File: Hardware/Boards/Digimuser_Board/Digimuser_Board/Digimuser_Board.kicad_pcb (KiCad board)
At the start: 2 copper layers, 63 parts, among them J1 Conn_01x01, J10 Conn_01x01, J11 Conn_01x01, J12 Conn_01x01, J2 Conn_01x01, J3 Barrel_Jack, J4 Conn_01x03, J5 Conn_01x03, J6 Conn_01x01, J7 Conn_01x01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

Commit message: Started the PCB layout. Also had to find a new voltage regulator.
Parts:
- removed H4: MountingHole_Pad, MountingHole:MountingHole_3.2mm_M3_Pad
- added C22: 0.33u, Capacitor_SMD:C_0805_2012Metric, F.Cu at (118.9, 69.3)
- added C23: 0.1u, Capacitor_SMD:C_0805_2012Metric, F.Cu at (121.2, 79.0)
- H1, H2, H3: footprint MountingHole:MountingHole_3.2mm_M3_Pad -> MountingHole:MountingHole_2.2mm_M2_Pad
- J3: value Barrel_Jack -> Barrel_Jack_MountingPin
- U2: value AMS1117CD-5.0 -> UA78M05IDCYR; footprint Package_TO_SOT_SMD:TO-252-3_TabPin2 -> Package_TO_SOT_SMD:SOT-223
- moved H1 80.9 mm to (165.7, 69.8)
- moved H2 65.8 mm to (165.7, 102.2)
- moved H3 31.2 mm to (104.8, 102.2)
- moved U2 7.67 mm to (123.4, 74.2)
- moved U4 6.43 mm to (120.0, 89.5)
- moved J3 6.30 mm to (115.6, 73.0)
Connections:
- J3 pad 1: Net-(J3-Pad1) -> Net-(C22-Pad1)
- J3 pad 3: (no net) -> GND
- U2 pad 1: GND -> Net-(C22-Pad1)
- U2 pad 2: 5V -> GND
- U2 pad 3: Net-(J3-Pad1) -> 5V
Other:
- board outline added: 67.3 x 38.7 mm

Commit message: Completed most of the PCB layout organization. Still have a lot of work on it.
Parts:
- J1: footprint Connector_PinSocket_2.54mm:PinSocket_1x01_P2.54mm_Vertical -> Connector_PinHeader_2.54mm:PinHeader_1x01_P2.54mm_Vertical
- J10, J11, J12, J6, J7, J8, J9: footprint Connector_Pin:Pin_D1.3mm_L11.0mm_LooseFit -> Connector_PinHeader_2.54mm:PinHeader_1x01_P2.54mm_Vertical
- U4: footprint teensy:Teensy40 -> teensy:Teensy40_HAT
- moved C1 89.2 mm to (130.3, 73.4), turned to 90 degrees
- moved R9 73.1 mm to (138.2, 73.7), turned to 180 degrees
- moved C14 68.0 mm to (146.8, 81.3), turned to 90 degrees
- moved R1 65.0 mm to (130.0, 76.5)
- moved C3 63.8 mm to (137.4, 70.4), turned to 90 degrees
- moved R6 63.4 mm to (134.1, 78.5), turned to 270 degrees
- moved C2 63.3 mm to (137.7, 79.2)
- moved J12 61.4 mm to (117.1, 102.1), turned to 90 degrees
- moved C4 61.4 mm to (148.1, 69.8), turned to 180 degrees
- moved U5 60.7 mm to (176.5, 100.2)
- moved R10 59.7 mm to (139.7, 70.4), turned to 270 degrees
- moved C6 58.3 mm to (149.9, 74.9), turned to 270 degrees
- moved C5 58.2 mm to (144.0, 78.0), turned to 180 degrees
- moved R2 57.6 mm to (131.1, 78.7), turned to 180 degrees
- moved C7 56.5 mm to (139.4, 96.4), turned to 270 degrees
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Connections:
- net Net-(C22-Pad1) renamed /+9V
- C16 pad 1: Net-(C16-Pad1) -> 3.3V
- C19 pad 1: Net-(C16-Pad1) -> 3.3V
- J3 pad 3: GND -> (no net)
- U4 pad 31: (no net) -> 3.3V
- U6 pad 4: (no net) -> MCLK
- U7 pad 9: Net-(C16-Pad1) -> 3.3V
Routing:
- net MCLK: track 0.00 -> 31.7 mm
- net SCLK: track 0.00 -> 25.9 mm
- net LRCK: track 0.00 -> 25.7 mm, vias 0 -> 1
- net 3.3V: track 0.00 -> 23.9 mm
- net SDOUT: track 0.00 -> 23.9 mm, vias 0 -> 1
- net 5V: track 0.00 -> 20.5 mm
- net Net-(C17-Pad1): track 0.00 -> 11.8 mm, vias 0 -> 2
- net Net-(J6-Pad1): track 0.00 -> 11.6 mm
- net /+9V: track 0.00 -> 9.03 mm
- net /FILT_OUT: track 0.00 -> 8.15 mm
- net ADC_IN: track 0.00 -> 7.47 mm
- net Net-(C15-Pad2): track 0.00 -> 5.39 mm
- net Net-(C11-Pad1): track 0.00 -> 4.28 mm
- net Net-(C5-Pad1): track 0.00 -> 4.20 mm
- net Net-(C6-Pad2): track 0.00 -> 2.56 mm
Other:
- net class 2_SIGNAL_SDSU_MILL added: clearance 0.2, trace_width 0.7, via_dia 1.4, via_drill 0.7
- net class JLCPWR added: clearance 0.3, trace_width 0.4, via_dia 1, via_drill 0.5
- net class PWR_SDSU_MILL added: clearance 0.9, trace_width 1.27, via_dia 1.4, via_drill 0.7
- net class SIGNAL_SDSU_MILL added: clearance 0.9, trace_width 0.7, via_dia 1.4, via_drill 0.7
- net class SMALLSIG added: clearance 0.1, trace_width 0.2, via_dia 0.5, via_drill 0.3

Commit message: Continued PCB layout.
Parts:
- C13: footprint Capacitor_THT:CP_Radial_D6.3mm_P2.50mm -> Capacitor_THT:C_Axial_L5.1mm_D3.1mm_P7.50mm_Horizontal
- U1: footprint Connector_PinSocket_2.54mm:PinSocket_1x04_P2.54mm_Vertical -> Connector_PinSocket_2.54mm:PinSocket_1x05_P2.54mm_Vertical
- moved R3 77.9 mm to (126.6, 85.9), turned to 270 degrees
- moved R4 76.5 mm to (128.9, 85.9), turned to 270 degrees
- moved R5 66.2 mm to (131.4, 85.9), turned to 270 degrees
- moved R7 65.8 mm to (134.0, 85.8), turned to 270 degrees
- moved R8 62.2 mm to (136.7, 85.8), turned to 270 degrees
- moved C12 51.8 mm to (145.3, 98.0), turned to 90 degrees
- moved J8 45.8 mm to (124.5, 102.1)
- moved R15 40.1 mm to (154.0, 100.1), turned to 90 degrees
- moved R17 39.9 mm to (150.8, 100.6)
- moved C9 39.7 mm to (153.0, 95.1), turned to 270 degrees
- moved U5 27.2 mm to (149.5, 97.0)
- moved U1 23.9 mm to (126.4, 78.9)
- moved J9 11.3 mm to (120.8, 102.1)
- moved C22 8.32 mm to (117.9, 77.6), turned to 270 degrees
- moved R14 7.74 mm to (159.8, 77.7), turned to 90 degrees
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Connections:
- U1 pad 1: Net-(R7-Pad1) -> Net-(R3-Pad1)
- U1 pad 2: Net-(R5-Pad1) -> Net-(R4-Pad1)
- U1 pad 3: Net-(R4-Pad1) -> Net-(R5-Pad1)
- U1 pad 4: Net-(R3-Pad1) -> Net-(R7-Pad1)
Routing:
- net 5V: track 20.5 -> 0.00 mm
- net Net-(C12-Pad1): track 0.00 -> 13.3 mm
- net DAC_OUT: track 0.00 -> 12.2 mm, vias 0 -> 2
- net /AMP_IN: track 0.00 -> 12.1 mm
- net Net-(C2-Pad1): track 0.00 -> 10.1 mm
- net Net-(C12-Pad2): track 0.00 -> 9.50 mm
- net /+9V: track 9.03 -> 0.13 mm
- net Net-(R15-Pad2): track 0.00 -> 6.34 mm
- net Net-(R5-Pad1): track 0.00 -> 6.13 mm
- net Net-(R4-Pad1): track 0.00 -> 6.13 mm
- net Net-(R3-Pad1): track 0.00 -> 6.10 mm
- net Net-(R7-Pad1): track 0.00 -> 6.04 mm
- net Net-(R8-Pad1): track 0.00 -> 5.97 mm
- net Net-(R10-Pad2): track 0.00 -> 5.55 mm
- net Net-(C10-Pad1): track 0.00 -> 5.10 mm
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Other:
- board size 67.3 x 38.7 mm -> 60.2 x 38.7 mm

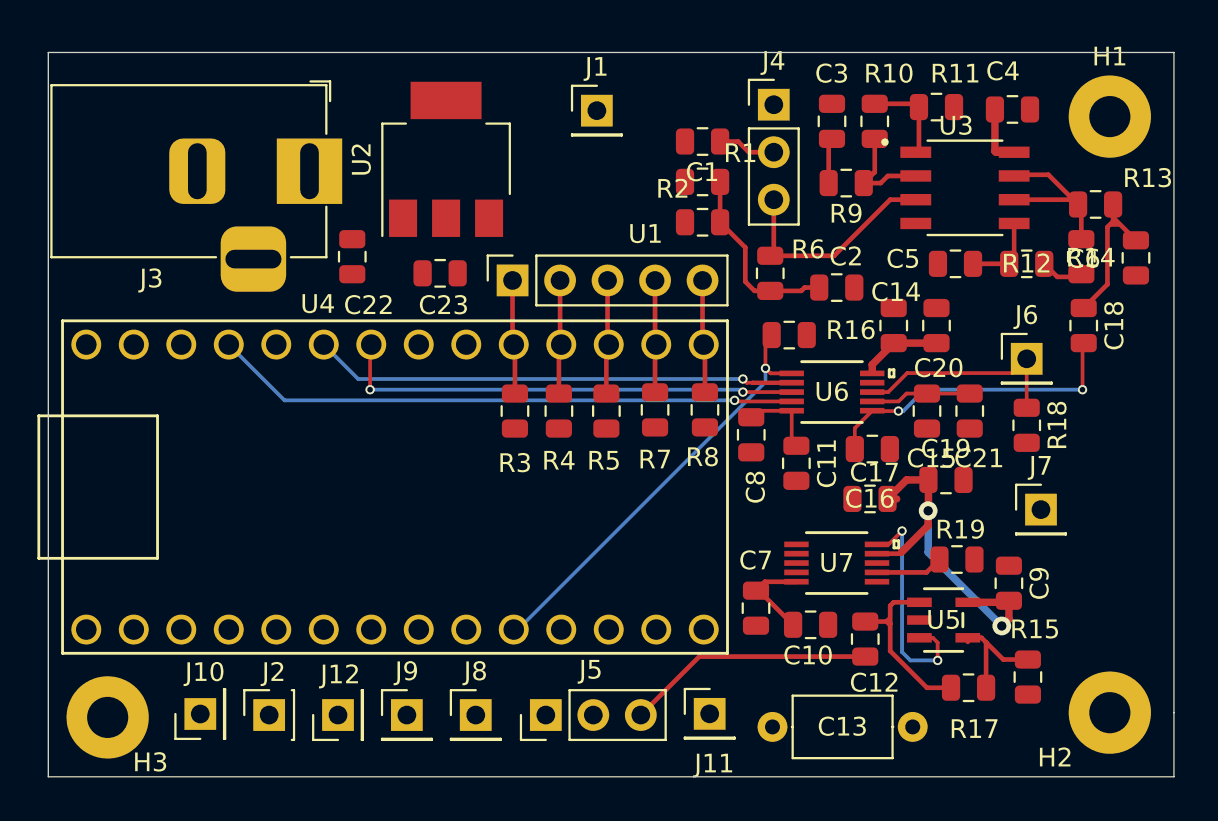
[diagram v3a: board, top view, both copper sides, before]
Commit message: Finished the first revision of the PCB layout. Needs reviewing.
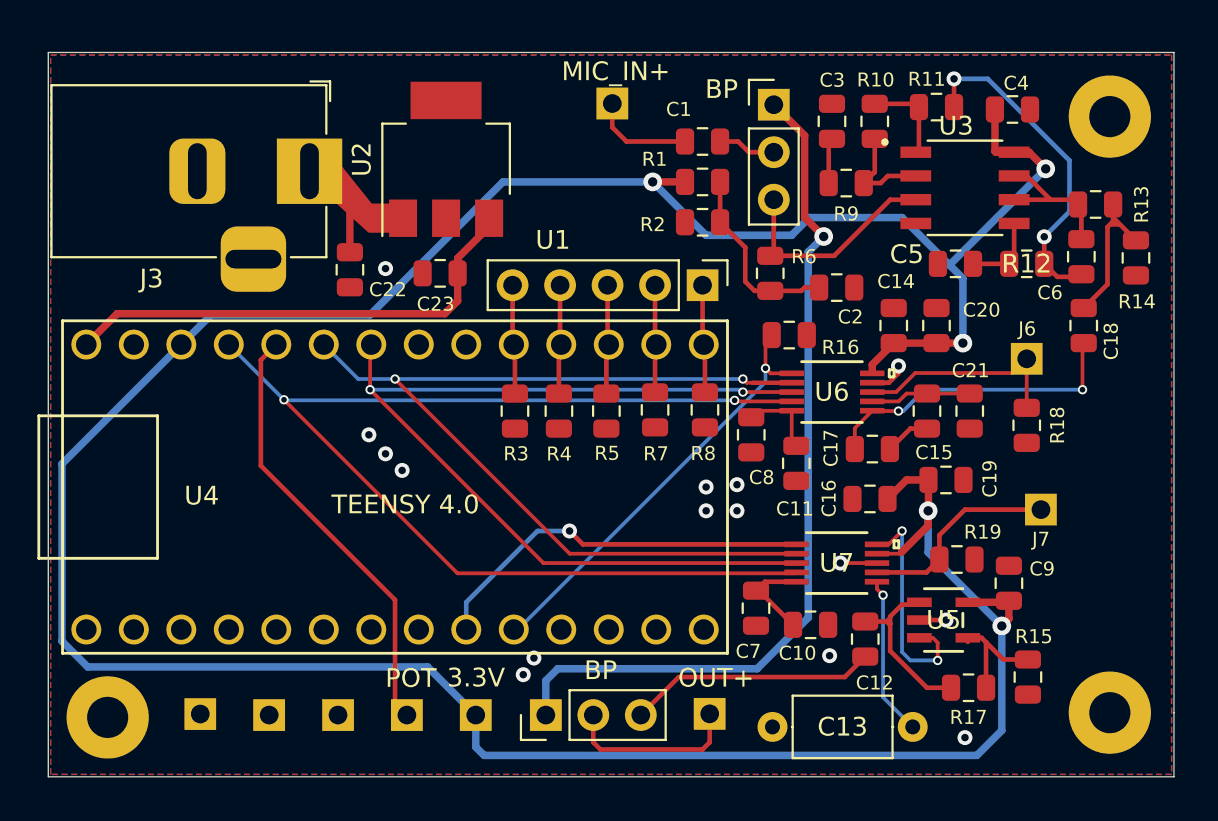
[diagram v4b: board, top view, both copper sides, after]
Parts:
- J1, J10, J11, J12, J6, J7, J8, J9: footprint Connector_PinHeader_2.54mm:PinHeader_1x01_P2.54mm_Vertical -> Custom_Connectors:PinHeader_2.54mm_1x01_P2.54mm
- J2: footprint Connector_PinSocket_2.54mm:PinSocket_1x01_P2.54mm_Vertical -> Custom_Connectors:PinHeader_2.54mm_1x01_P2.54mm
- J4, J5: footprint Connector_PinHeader_2.54mm:PinHeader_1x03_P2.54mm_Vertical -> Custom_Connectors:PinHeader_2.54mm_1x03_P2.54mm
- U1: footprint Connector_PinSocket_2.54mm:PinSocket_1x05_P2.54mm_Vertical -> Custom_Connectors:R20407RR02Q
- U7: value CS4344-CZZ -> (none)
- moved U1 10.2 mm to (136.6, 79.1), turned to 270 degrees
- moved J1 0.91 mm to (131.8, 69.4)
- moved C22 0.71 mm to (117.7, 78.3)
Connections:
- U1 pad 1: Net-(R3-Pad1) -> Net-(R7-Pad1)
- U1 pad 2: Net-(R4-Pad1) -> Net-(R5-Pad1)
- U1 pad 3: Net-(R5-Pad1) -> Net-(R4-Pad1)
- U1 pad 4: Net-(R7-Pad1) -> Net-(R3-Pad1)
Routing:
- net 3.3V: track 27.9 -> 170.2 mm, vias 2 -> 5
- net BYPASS: track 0.00 -> 46.1 mm, vias 0 -> 1
- net MCLK: track 31.4 -> 62.6 mm, vias 1 -> 2
- net LRCK: track 25.1 -> 51.7 mm
- net 5V: track 0.00 -> 25.9 mm
- net SCLK: track 27.3 -> 52.6 mm, vias 1 -> 2
- net Net-(J9-Pad1): track 0.00 -> 23.4 mm
- net SDIN: track 0.00 -> 21.0 mm, vias 0 -> 1
- net Net-(C6-Pad2): track 2.33 -> 18.0 mm, vias 0 -> 2
- net /+9V: track 0.13 -> 10.5 mm
- net Net-(J11-Pad1): track 0.00 -> 9.52 mm
- net Net-(C13-Pad1): track 0.00 -> 8.55 mm, vias 0 -> 1
- net GND: track 0.00 -> 7.82 mm, vias 0 -> 15
- net Net-(J7-Pad1): track 3.62 -> 10.9 mm
- net Net-(C1-Pad2): track 0.00 -> 5.47 mm
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- added copper zone on B.Cu, net GND
- added copper zone on F.Cu, net GND
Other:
- net class JLCPWR: clearance 0.3 -> 0.2
- board text added: "3.3V"
- board text added: "BP"
- board text added: "MIC_IN+"
- board text added: "OUT+"
- board text added: "POT"
- board text added: "TEENSY 4.0"

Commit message: Did a re-layout of the PCB and redid the schematic.Ready for review.
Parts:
- removed U5: MCP6271T-E_OT, MCP6271TE0T:MCP6271T-E&slash_OT
- added C24: 3.9n, Capacitor_SMD:C_0805_2012Metric, F.Cu at (157.3, 91.8)
- added C25: 3.9n, Capacitor_SMD:C_0805_2012Metric, F.Cu at (157.4, 95.5)
- added C26: 1u, Capacitor_SMD:C_0805_2012Metric, F.Cu at (155.2, 81.9)
- added C27: 180p, Capacitor_SMD:C_0805_2012Metric, F.Cu at (152.5, 81.9)
- added TP1: FILTIN, TestPoint:TestPoint_Keystone_5019_Minature, B.Cu at (146.8, 71.6)
- added TP2: FILTOUT, TestPoint:TestPoint_Keystone_5019_Minature, B.Cu at (153.6, 78.7)
- added TP3: AOUTR, TestPoint:TestPoint_Keystone_5019_Minature, B.Cu at (145.4, 89.7)
- added TP4: AOUTL, TestPoint:TestPoint_Keystone_5019_Minature, B.Cu at (146.3, 96.5)
- C12: value ? -> 3.3u
- C9: value 0.1u -> 3.3u
- R15: value 1K -> 10K
- R17: value 5K -> 10K
- R18: value 0 -> 470
- R19: value 10K -> 470
- U7: value (none) -> CS4344-CZZ
- moved J11 8.85 mm to (128.1, 102.1)
- moved R15 8.26 mm to (153.3, 91.8)
- moved J5 7.33 mm to (135.5, 102.1)
- moved C12 5.99 mm to (150.4, 94.9), turned to 180 degrees
- moved J7 5.92 mm to (158.9, 86.9)
- moved R17 5.70 mm to (153.3, 95.5), turned to 270 degrees
- moved R18 5.41 mm to (155.3, 91.8)
- moved R19 5.38 mm to (155.3, 95.5), turned to 90 degrees
- moved J6 4.06 mm to (155.2, 86.9)
- moved C13 3.78 mm to (146.6, 99.2), turned to 0 degrees
- moved C9 3.42 mm to (150.4, 92.8), turned to 180 degrees
- moved C18 0.66 mm to (157.6, 81.2)
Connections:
- C9 pad 1: GND -> Net-(C9-Pad1)
- C9 pad 2: 3.3V -> Net-(C9-Pad2)
- J5 pad 3: Net-(C12-Pad1) -> Net-(C25-Pad1)
- J6 pad 1: Net-(J6-Pad1) -> Net-(C26-Pad1)
- J7 pad 1: Net-(J7-Pad1) -> Net-(C24-Pad1)
- R15 pad 1: GND -> Net-(C9-Pad1)
- R15 pad 2: Net-(R15-Pad2) -> GND
- R17 pad 1: Net-(C12-Pad2) -> Net-(C12-Pad1)
- R17 pad 2: Net-(R15-Pad2) -> GND
- R18 pad 1: Net-(J6-Pad1) -> Net-(C24-Pad1)
- R18 pad 2: GND -> Net-(C9-Pad1)
- R19 pad 1: Net-(J7-Pad1) -> Net-(C25-Pad1)
- R19 pad 2: GND -> Net-(C12-Pad1)
- U6 pad 8: Net-(J6-Pad1) -> Net-(C26-Pad2)
- U7 pad 10: DAC_OUT -> Net-(C9-Pad2)
- U7 pad 7: Net-(J7-Pad1) -> Net-(C12-Pad2)
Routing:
- net Net-(C25-Pad1): track 0.00 -> 21.7 mm
- net DAC_OUT: track 12.2 -> 0.00 mm, vias 2 -> 0
- net Net-(C26-Pad2): track 0.00 -> 12.0 mm
- net Net-(J6-Pad1): track 11.6 -> 0.00 mm
- net Net-(J7-Pad1): track 10.9 -> 0.00 mm
- net BYPASS: track 46.1 -> 36.8 mm
- net Net-(C12-Pad1): track 13.3 -> 4.20 mm
- net Net-(C9-Pad2): track 0.00 -> 8.10 mm, vias 0 -> 1
- net Net-(C24-Pad1): track 0.00 -> 6.65 mm
- net Net-(R15-Pad2): track 6.34 -> 0.00 mm
- net /FILT_IN: track 4.92 -> 9.94 mm, vias 0 -> 1
- net /FILT_OUT: track 8.01 -> 13.0 mm, vias 0 -> 1
- net Net-(C26-Pad1): track 0.00 -> 4.11 mm
- net Net-(C13-Pad1): track 8.55 -> 4.47 mm, vias 1 -> 0
- net Net-(C9-Pad1): track 0.00 -> 3.93 mm
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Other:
- board text added: "GND"

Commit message: Relabled Testpoints on PCB.
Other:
- board text added: "AOUTL"
- board text added: "AOUTR"
- board text added: "FILTIN"
- board text added: "FILTOUT"

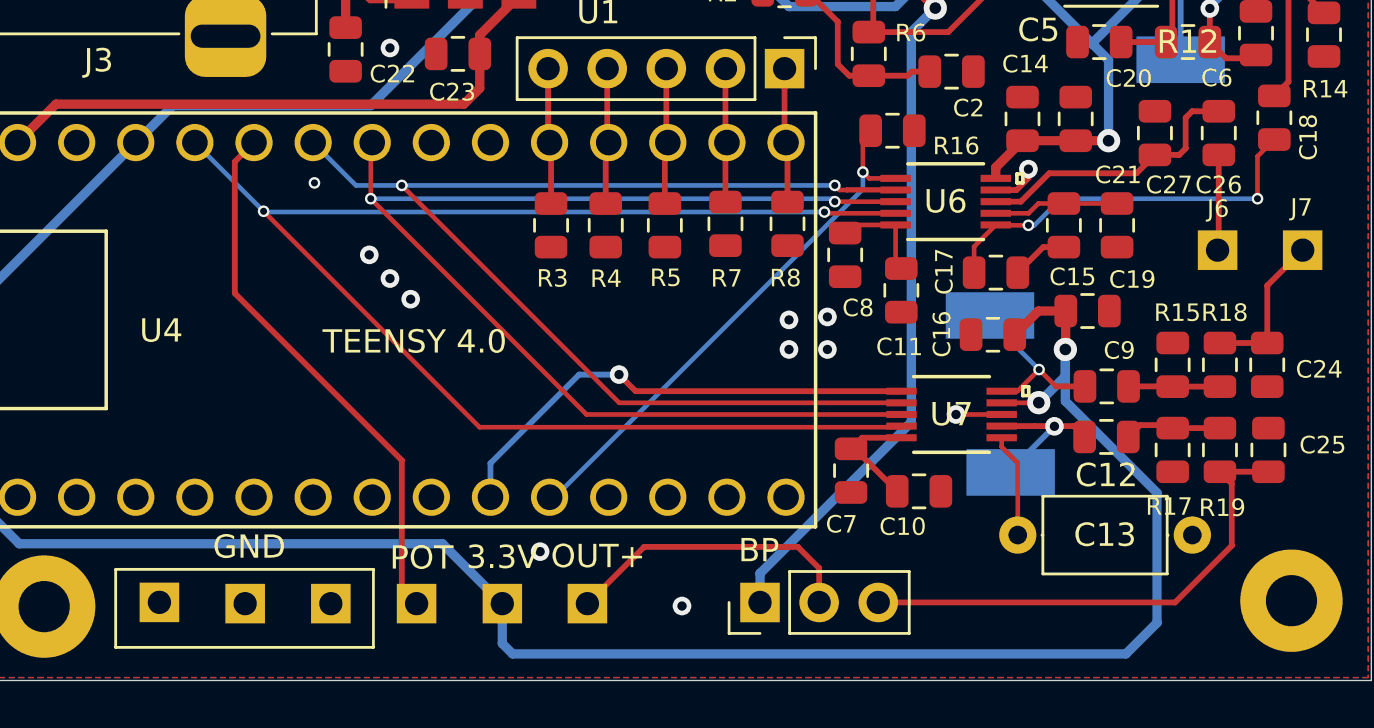
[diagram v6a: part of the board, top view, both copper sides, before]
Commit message: Added pin connection for a second potentiometer.
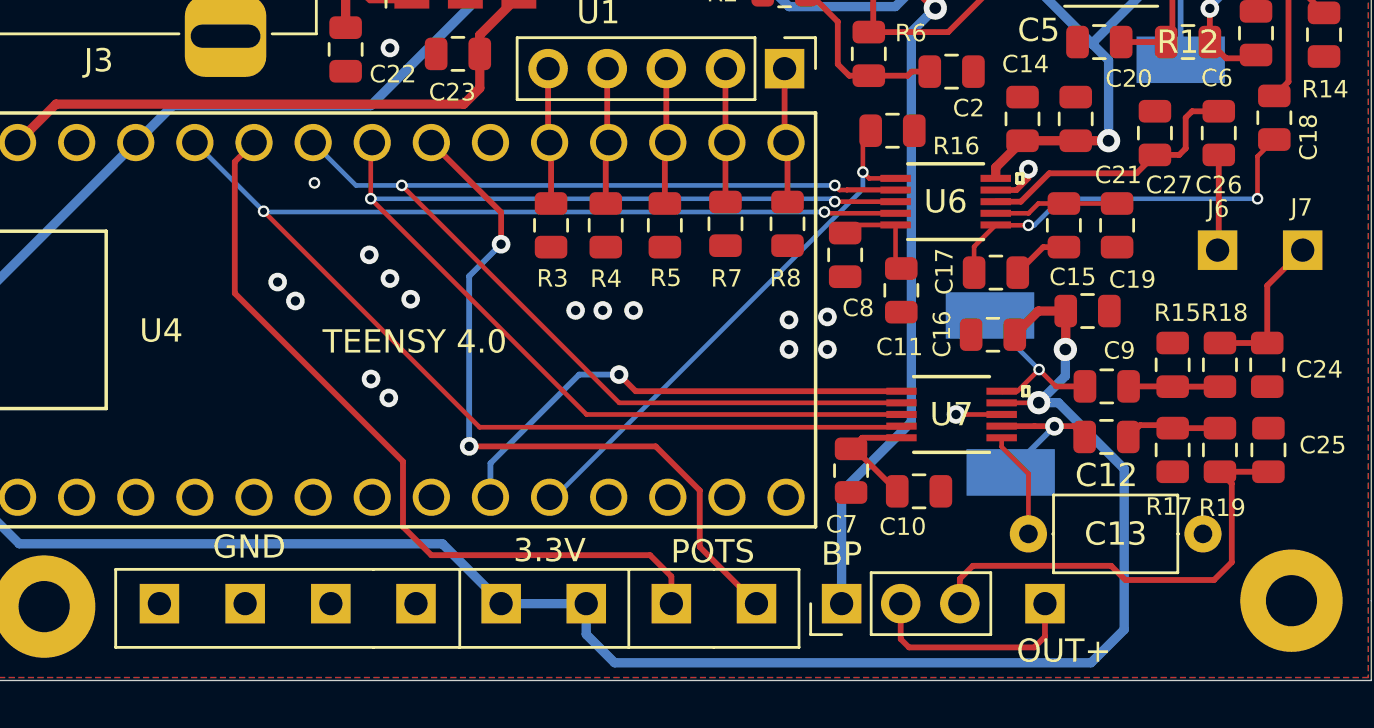
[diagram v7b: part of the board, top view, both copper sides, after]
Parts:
- added J13: Conn_01x01, Custom_Connectors:PinHeader_2.54mm_1x01_P2.54mm, F.Cu at (128.1, 102.1)
- added J14: Conn_01x01, Custom_Connectors:PinHeader_2.54mm_1x01_P2.54mm, F.Cu at (120.8, 102.1)
- added J15: Conn_01x01, Custom_Connectors:PinHeader_2.54mm_1x01_P2.54mm, F.Cu at (135.4, 102.1)
- moved J11 19.7 mm to (147.8, 102.1)
- moved J9 10.9 mm to (131.7, 102.1)
- moved J5 3.51 mm to (139.0, 102.1)
- moved C13 0.46 mm to (147.1, 99.1)
- moved J10 0.06 mm to (109.7, 102.1)
- moved J8 0.05 mm to (124.4, 102.1)
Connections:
- U4 pad 26: (no net) -> Net-(J15-Pad1)
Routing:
- net Net-(J15-Pad1): track 0.00 -> 31.4 mm, vias 0 -> 2
- net Net-(J9-Pad1): track 23.4 -> 33.4 mm
- net Net-(J11-Pad1): track 12.8 -> 9.48 mm
- net 3.3V: track 166.4 -> 163.4 mm
- net Net-(C25-Pad1): track 21.7 -> 19.7 mm
- net BYPASS: track 36.8 -> 35.4 mm
- net GND: vias 16 -> 21
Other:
- board text added: "POTS"
- board text removed: "POT"
